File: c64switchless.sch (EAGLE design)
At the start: 12 parts, among them IC1 27C256, IC2 PIC12F629P, X1 B4B-ZR

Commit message: Revision + silkscreen text
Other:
- note added: "Rev 1"
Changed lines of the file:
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@@
 <text x="165.1" y="17.78" size="1.778" layer="91">adapter with switchless multikernal switch</text>
 <text x="165.1" y="10.16" size="1.778" layer="91">Design by BWACK</text>
+<text x="247.65" y="5.334" size="1.778" layer="91">Rev 1</text>
 </plain>
 <instances>

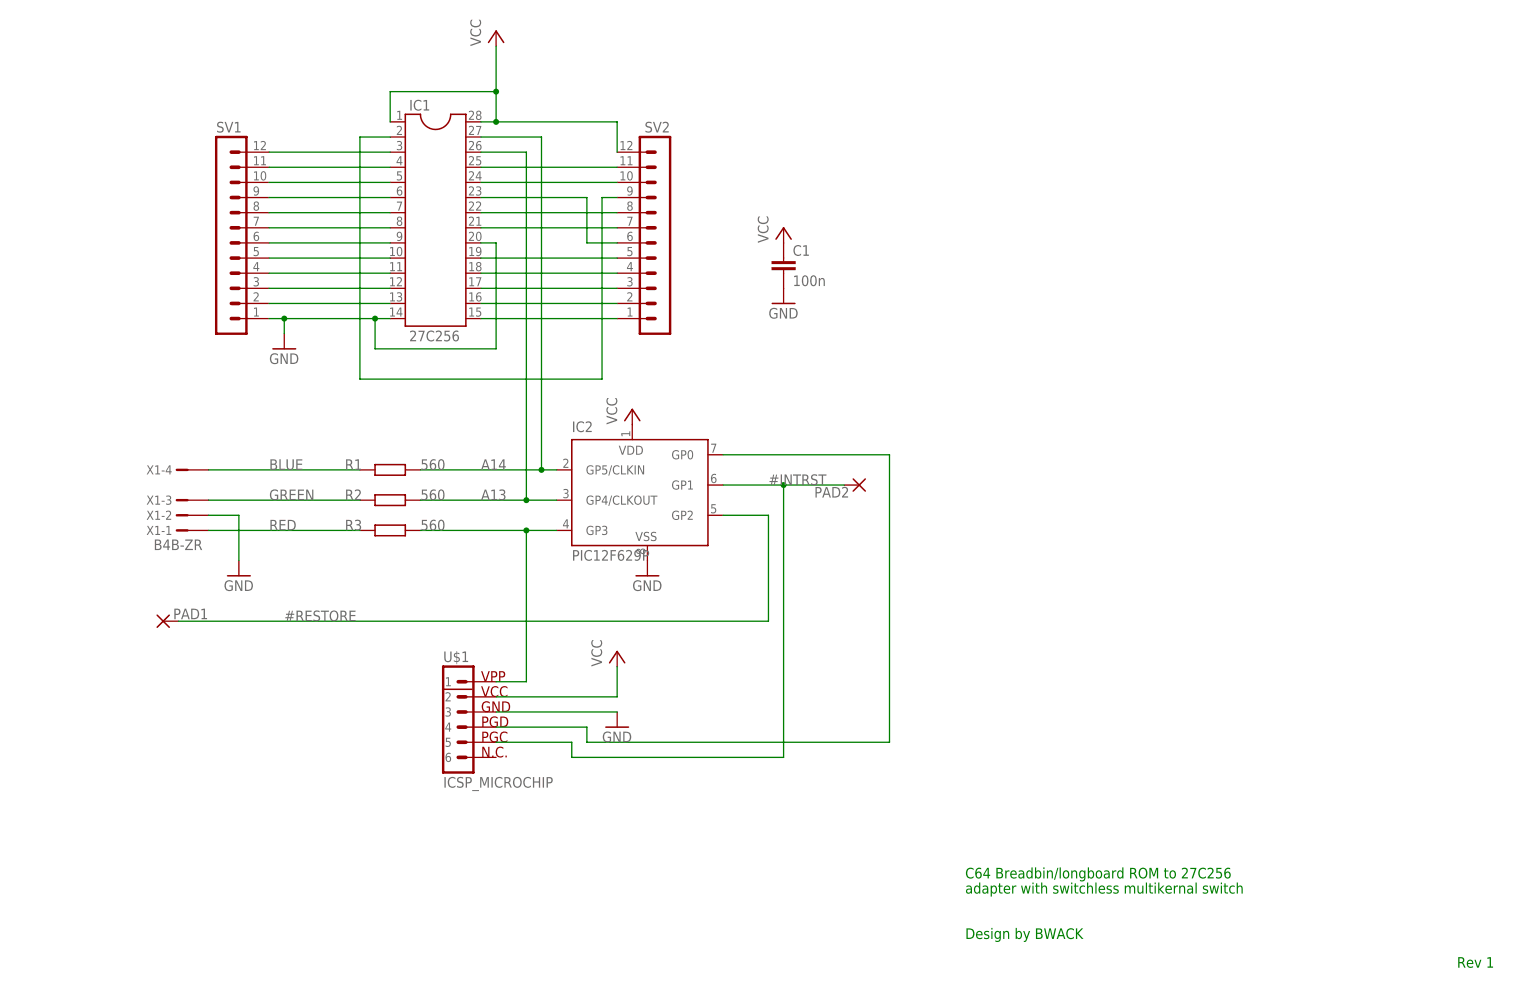
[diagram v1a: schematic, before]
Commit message: swapped LED and RESTORE on GP2 and GP3
GP3 is the fekken input only pin
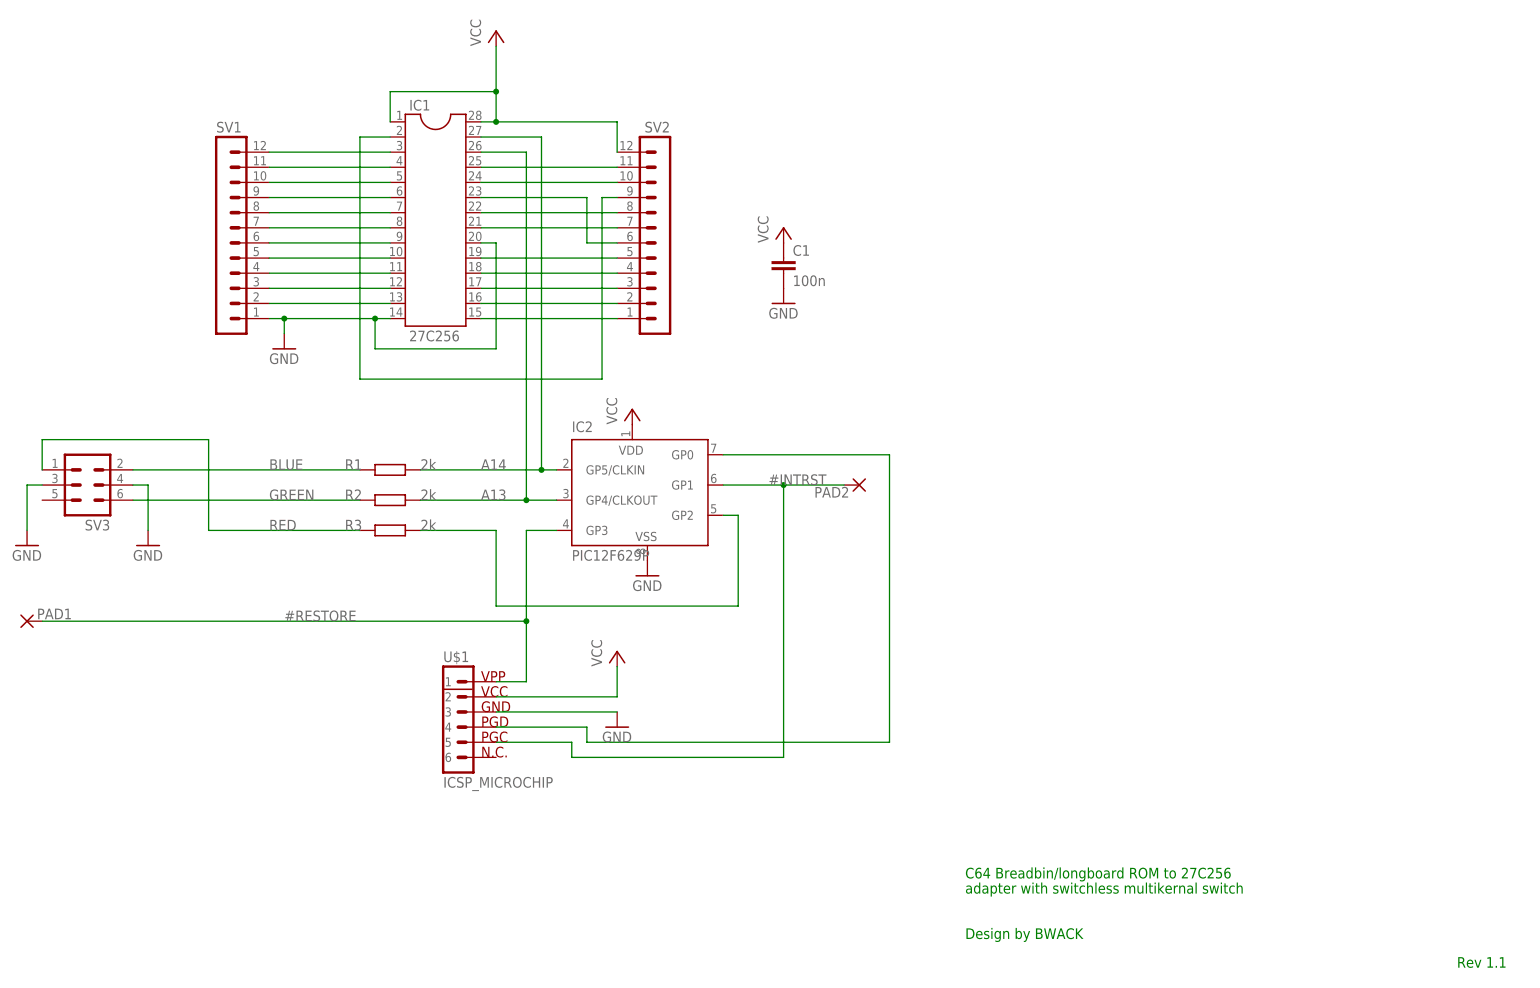
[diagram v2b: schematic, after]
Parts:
- removed X1: B4B-ZR, con-jst:B4B-ZR
- added SV3: (no value), con-lstb:MA03-2
- R1, R2, R3: value 560 -> 2k; device rcl:R-EU_0204/7 -> rcl:R-EU_0207/10
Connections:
- removed net N$25: IC2.GP3, R3.2, U$1.1
- new net N$22: IC2.GP2, R3.2
- net #RESTORE: now also IC2.GP3, U$1.1; no longer IC2.GP2
- net BLUE: now also SV3.2; no longer X1-4.1
- net GND: now also SV3.3, SV3.4; no longer X1-2.1
- net GREEN: now also SV3.6; no longer X1-3.1
- net RED: now also SV3.1; no longer X1-1.1
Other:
- note added: "Rev 1.1"
- note removed: "Rev 1"
- moved on the sheet: PAD1

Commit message: Sch+Layout changed to match RGB LEDs pinout
See readme.txt
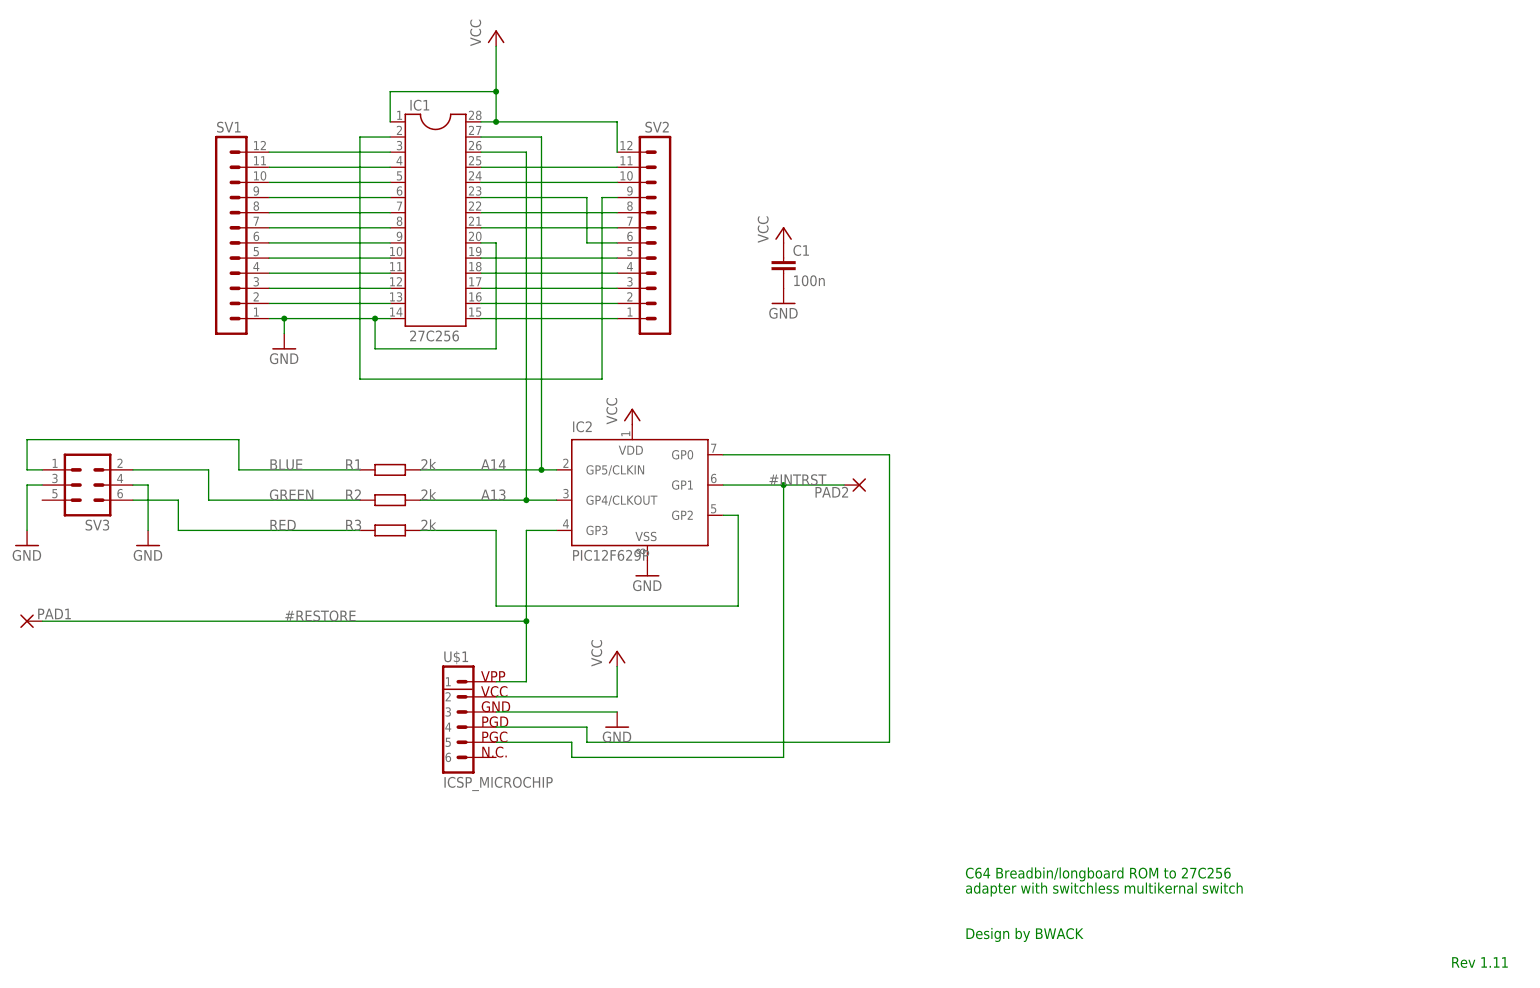
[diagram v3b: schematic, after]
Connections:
- net BLUE: now also SV3.1; no longer SV3.2
- net GREEN: now also SV3.2; no longer SV3.6
- net RED: now also SV3.6; no longer SV3.1
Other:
- note added: "Rev 1.11"
- note removed: "Rev 1.1"
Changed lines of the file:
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@@
 <grid distance="0.1" unitdist="inch" unit="inch" style="lines" multiple="1" display="no" altdistance="0.01" altunitdist="inch" altunit="inch"/>
 <layers>
-<layer number="1" name="Top" color="4" fill="1" visible="yes" active="no"/>
-<layer number="2" name="Route2" color="1" fill="3" visible="yes" active="no"/>
-<layer number="3" name="Route3" color="4" fill="3" visible="yes" active="no"/>
-<layer number="4" name="Route4" color="1" fill="4" visible="yes" active="no"/>
-<layer number="5" name="Route5" color="4" fill="4" visible="yes" active="no"/>
-<layer number="6" name="Route6" color="1" fill="8" visible="yes" active="no"/>
-<layer number="7" name="Route7" color="4" fill="8" visible="yes" active="no"/>
-<layer number="8" name="Route8" color="1" fill="2" visible="yes" active="no"/>
-<layer number="9" name="Route9" color="4" fill="2" visible="yes" active="no"/>
-<layer number="10" name="Route10" color="1" fill="7" visible="yes" active="no"/>
-<layer number="11" name="Route11" color="4" fill="7" visible="yes" active="no"/>
-<layer number="12" name="Route12" color="1" fill="5" visible="yes" active="no"/>
-<layer number="13" name="Route13" color="4" fill="5" visible="yes" active="no"/>
-<layer number="14" name="Route14" color="1" fill="6" visible="yes" active="no"/>
-<layer number="15" name="Route15" color="4" fill="6" visible="yes" active="no"/>
-<layer number="16" name="Bottom" color="1" fill="1" visible="yes" active="no"/>
-<layer number="17" name="Pads" color="2" fill="1" visible="yes" active="no"/>
-<layer number="18" name="Vias" color="2" fill="1" visible="yes" active="no"/>
-<layer number="19" name="Unrouted" color="6" fill="1" visible="yes" active="no"/>
-<layer number="20" name="Dimension" color="15" fill="1" visible="yes" active="no"/>
-<layer number="21" name="tPlace" color="7" fill="1" visible="yes" active="no"/>
-<layer number="22" name="bPlace" color="7" fill="1" visible="yes" active="no"/>
-<layer number="23" name="tOrigins" color="15" fill="1" visible="yes" active="no"/>
-<layer number="24" name="bOrigins" color="15" fill="1" visible="yes" active="no"/>
-<layer number="25" name="tNames" color="7" fill="1" visible="yes" active="no"/>
-<layer number="26" name="bNames" color="7" fill="1" visible="yes" active="no"/>
-<layer number="27" name="tValues" color="7" fill="1" visible="yes" active="no"/>
-<layer number="28" name="bValues" color="7" fill="1" visible="yes" active="no"/>
+<layer number="1" name="Top" color="4" fill="1" visible="no" active="no"/>
+<layer number="2" name="Route2" color="1" fill="3" visible="no" active="no"/>
+<layer number="3" name="Route3" color="4" fill="3" visible="no" active="no"/>
+<layer number="4" name="Route4" color="1" fill="4" visible="no" active="no"/>
+<layer number="5" name="Route5" color="4" fill="4" visible="no" active="no"/>
+<layer number="6" name="Route6" color="1" fill="8" visible="no" active="no"/>
+<layer number="7" name="Route7" color="4" fill="8" visible="no" active="no"/>
+<layer number="8" name="Route8" color="1" fill="2" visible="no" active="no"/>
+<layer number="9" name="Route9" color="4" fill="2" visible="no" active="no"/>
+<layer number="10" name="Route10" color="1" fill="7" visible="no" active="no"/>
+<layer number="11" name="Route11" color="4" fill="7" visible="no" active="no"/>
+<layer number="12" name="Route12" color="1" fill="5" visible="no" active="no"/>
+<layer number="13" name="Route13" color="4" fill="5" visible="no" active="no"/>
+<layer number="14" name="Route14" color="1" fill="6" visible="no" active="no"/>
+<layer number="15" name="Route15" color="4" fill="6" visible="no" active="no"/>
+<layer number="16" name="Bottom" color="1" fill="1" visible="no" active="no"/>
+<layer number="17" name="Pads" color="2" fill="1" visible="no" active="no"/>
+<layer number="18" name="Vias" color="2" fill="1" visible="no" active="no"/>
+<layer number="19" name="Unrouted" color="6" fill="1" visible="no" active="no"/>
+<layer number="20" name="Dimension" color="15" fill="1" visible="no" active="no"/>
+<layer number="21" name="tPlace" color="7" fill="1" visible="no" active="no"/>
+<layer number="22" name="bPlace" color="7" fill="1" visible="no" active="no"/>
+<layer number="23" name="tOrigins" color="15" fill="1" visible="no" active="no"/>
+<layer number="24" name="bOrigins" color="15" fill="1" visible="no" active="no"/>
+<layer number="25" name="tNames" color="7" fill="1" visible="no" active="no"/>
+<layer number="26" name="bNames" color="7" fill="1" visible="no" active="no"/>
+<layer number="27" name="tValues" color="7" fill="1" visible="no" active="no"/>
+<layer number="28" name="bValues" color="7" fill="1" visible="no" active="no"/>
 <layer number="29" name="tStop" color="7" fill="3" visible="no" active="no"/>
 <layer number="30" name="bStop" color="7" fill="6" visible="no" active="no"/>
@@
 <layer number="35" name="tGlue" color="7" fill="4" visible="no" active="no"/>
 <layer number="36" name="bGlue" color="7" fill="5" visible="no" active="no"/>
-<layer number="37" name="tTest" color="7" fill="1" visible="yes" active="no"/>
-<layer number="38" name="bTest" color="7" fill="1" visible="yes" active="no"/>
+<layer number="37" name="tTest" color="7" fill="1" visible="no" active="no"/>
+<layer number="38" name="bTest" color="7" fill="1" visible="no" active="no"/>
 <layer number="39" name="tKeepout" color="4" fill="11" visible="no" active="no"/>
 <layer number="40" name="bKeepout" color="1" fill="11" visible="no" active="no"/>
@@
 <layer number="44" name="Drills" color="7" fill="1" visible="no" active="no"/>
 <layer number="45" name="Holes" color="7" fill="1" visible="no" active="no"/>
-<layer number="46" name="Milling" color="3" fill="1" visible="yes" active="no"/>
-<layer number="47" name="Measures" color="7" fill="1" visible="yes" active="no"/>
-<layer number="48" name="Document" color="7" fill="1" visible="yes" active="no"/>
-<layer number="49" name="Reference" color="7" fill="1" visible="yes" active="no"/>
-<layer number="51" name="tDocu" color="7" fill="1" visible="yes" active="no"/>
-<layer number="52" name="bDocu" color="7" fill="1" visible="yes" active="no"/>
+<layer number="46" name="Milling" color="3" fill="1" visible="no" active="no"/>
+<layer number="47" name="Measures" color="7" fill="1" visible="no" active="no"/>
+<layer number="48" name="Document" color="7" fill="1" visible="no" active="no"/>
+<layer number="49" name="Reference" color="7" fill="1" visible="no" active="no"/>
+<layer number="51" name="tDocu" color="7" fill="1" visible="no" active="no"/>
+<layer number="52" name="bDocu" color="7" fill="1" visible="no" active="no"/>
 <layer number="91" name="Nets" color="2" fill="1" visible="yes" active="yes"/>
 <layer number="92" name="Busses" color="1" fill="1" visible="yes" active="yes"/>
@@
 <text x="165.1" y="17.78" size="1.778" layer="91">adapter with switchless multikernal switch</text>
 <text x="165.1" y="10.16" size="1.778" layer="91">Design by BWACK</text>
-<text x="247.65" y="5.334" size="1.778" layer="91">Rev 1.1</text>
+<text x="246.634" y="5.334" size="1.778" layer="91">Rev 1.11</text>
 </plain>
 <instances>
@@
 </segment>
 </net>
-<net name="GREEN" class="0">
-<segment>
-<pinref part="R2" gate="G$1" pin="1"/>
-<wire x1="63.5" y1="83.82" x2="25.4" y2="83.82" width="0.1524" layer="91"/>
-<label x="48.26" y="83.82" size="1.778" layer="95"/>
-<pinref part="SV3" gate="1" pin="6"/>
-</segment>
-</net>
 <net name="BLUE" class="0">
 <segment>
 <pinref part="R1" gate="G$1" pin="1"/>
-<wire x1="63.5" y1="88.9" x2="25.4" y2="88.9" width="0.1524" layer="91"/>
+<wire x1="63.5" y1="88.9" x2="43.18" y2="88.9" width="0.1524" layer="91"/>
 <label x="48.26" y="88.9" size="1.778" layer="95"/>
-<pinref part="SV3" gate="1" pin="2"/>
+<pinref part="SV3" gate="1" pin="1"/>
+<wire x1="10.16" y1="88.9" x2="7.62" y2="88.9" width="0.1524" layer="91"/>
+<wire x1="7.62" y1="88.9" x2="7.62" y2="93.98" width="0.1524" layer="91"/>
+<wire x1="7.62" y1="93.98" x2="43.18" y2="93.98" width="0.1524" layer="91"/>
+<wire x1="43.18" y1="93.98" x2="43.18" y2="88.9" width="0.1524" layer="91"/>
 </segment>
 </net>
@@
 <segment>
 <pinref part="R3" gate="G$1" pin="1"/>
-<wire x1="38.1" y1="78.74" x2="63.5" y2="78.74" width="0.1524" layer="91"/>
+<wire x1="33.02" y1="78.74" x2="63.5" y2="78.74" width="0.1524" layer="91"/>
 <label x="48.26" y="78.74" size="1.778" layer="95"/>
-<wire x1="38.1" y1="78.74" x2="38.1" y2="93.98" width="0.1524" layer="91"/>
-<wire x1="38.1" y1="93.98" x2="10.16" y2="93.98" width="0.1524" layer="91"/>
-<pinref part="SV3" gate="1" pin="1"/>
-<wire x1="10.16" y1="93.98" x2="10.16" y2="88.9" width="0.1524" layer="91"/>
+<pinref part="SV3" gate="1" pin="6"/>
+<wire x1="33.02" y1="78.74" x2="33.02" y2="83.82" width="0.1524" layer="91"/>
+<wire x1="33.02" y1="83.82" x2="25.4" y2="83.82" width="0.1524" layer="91"/>
 </segment>
 </net>
@@
 </segment>
 </net>
+<net name="GREEN" class="0">
+<segment>
+<pinref part="R2" gate="G$1" pin="1"/>
+<wire x1="63.5" y1="83.82" x2="38.1" y2="83.82" width="0.1524" layer="91"/>
+<wire x1="38.1" y1="83.82" x2="38.1" y2="88.9" width="0.1524" layer="91"/>
+<pinref part="SV3" gate="1" pin="2"/>
+<wire x1="38.1" y1="88.9" x2="25.4" y2="88.9" width="0.1524" layer="91"/>
+<label x="48.26" y="83.82" size="1.778" layer="95"/>
+</segment>
+</net>

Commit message: updated with license
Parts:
- renumbered U$1 to SV4
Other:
- note added: "CERN OPEN HARDWARE LICENSE v1.2"
- note added: "http://www.ohwr.org/"
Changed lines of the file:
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@@
 <part name="GND1" library="supply1" deviceset="GND" device=""/>
 <part name="GND2" library="supply1" deviceset="GND" device=""/>
-<part name="U$1" library="microchip" deviceset="ICSP_MICROCHIP" device=""/>
+<part name="SV4" library="microchip" deviceset="ICSP_MICROCHIP" device=""/>
 <part name="P+3" library="supply1" deviceset="VCC" device=""/>
 <part name="GND3" library="supply1" deviceset="GND" device=""/>
@@
 <text x="165.1" y="20.32" size="1.778" layer="91">C64 Breadbin/longboard ROM to 27C256</text>
 <text x="165.1" y="17.78" size="1.778" layer="91">adapter with switchless multikernal switch</text>
-<text x="165.1" y="10.16" size="1.778" layer="91">Design by BWACK</text>
+<text x="165.1" y="12.7" size="1.778" layer="91">Design by BWACK</text>
 <text x="246.634" y="5.334" size="1.778" layer="91">Rev 1.11</text>
+<text x="165.1" y="5.08" size="1.778" layer="91">http://www.ohwr.org/</text>
+<text x="165.1" y="7.62" size="1.778" layer="91">CERN OPEN HARDWARE LICENSE v1.2</text>
 </plain>
 <instances>
@@
 <instance part="GND1" gate="1" x="134.62" y="116.84"/>
 <instance part="GND2" gate="1" x="50.8" y="109.22"/>
-<instance part="U$1" gate="G$1" x="78.74" y="45.72"/>
+<instance part="SV4" gate="G$1" x="78.74" y="45.72"/>
 <instance part="P+3" gate="VCC" x="106.68" y="58.42"/>
 <instance part="GND3" gate="1" x="106.68" y="45.72"/>
@@
 <segment>
 <pinref part="GND3" gate="1" pin="GND"/>
-<pinref part="U$1" gate="G$1" pin="3"/>
+<pinref part="SV4" gate="G$1" pin="3"/>
 <wire x1="106.68" y1="48.26" x2="86.36" y2="48.26" width="0.1524" layer="91"/>
 </segment>
@@
 </segment>
 <segment>
-<pinref part="U$1" gate="G$1" pin="2"/>
+<pinref part="SV4" gate="G$1" pin="2"/>
 <pinref part="P+3" gate="VCC" pin="VCC"/>
 <wire x1="86.36" y1="50.8" x2="106.68" y2="50.8" width="0.1524" layer="91"/>
@@
 <pinref part="PAD2" gate="G$1" pin="P"/>
 <label x="132.08" y="86.36" size="1.778" layer="95"/>
-<pinref part="U$1" gate="G$1" pin="5"/>
+<pinref part="SV4" gate="G$1" pin="5"/>
 <wire x1="134.62" y1="86.36" x2="144.78" y2="86.36" width="0.1524" layer="91"/>
 <wire x1="86.36" y1="43.18" x2="99.06" y2="43.18" width="0.1524" layer="91"/>
@@
 <label x="50.8" y="63.5" size="1.778" layer="95"/>
 <wire x1="91.44" y1="63.5" x2="10.16" y2="63.5" width="0.1524" layer="91"/>
-<pinref part="U$1" gate="G$1" pin="1"/>
+<pinref part="SV4" gate="G$1" pin="1"/>
 <wire x1="86.36" y1="53.34" x2="91.44" y2="53.34" width="0.1524" layer="91"/>
 <pinref part="IC2" gate="G$1" pin="GP3"/>
@@
 <net name="N$1" class="0">
 <segment>
-<pinref part="U$1" gate="G$1" pin="4"/>
+<pinref part="SV4" gate="G$1" pin="4"/>
 <wire x1="86.36" y1="45.72" x2="101.6" y2="45.72" width="0.1524" layer="91"/>
 <wire x1="101.6" y1="45.72" x2="101.6" y2="43.18" width="0.1524" layer="91"/>
